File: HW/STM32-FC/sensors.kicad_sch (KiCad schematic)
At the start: 18 parts, among them J5 JST ZH 1.5mm 2P, U6 BMI323, U7 ICM-42688-P, U8 LIS2MDLTR, U9 LPS22HH

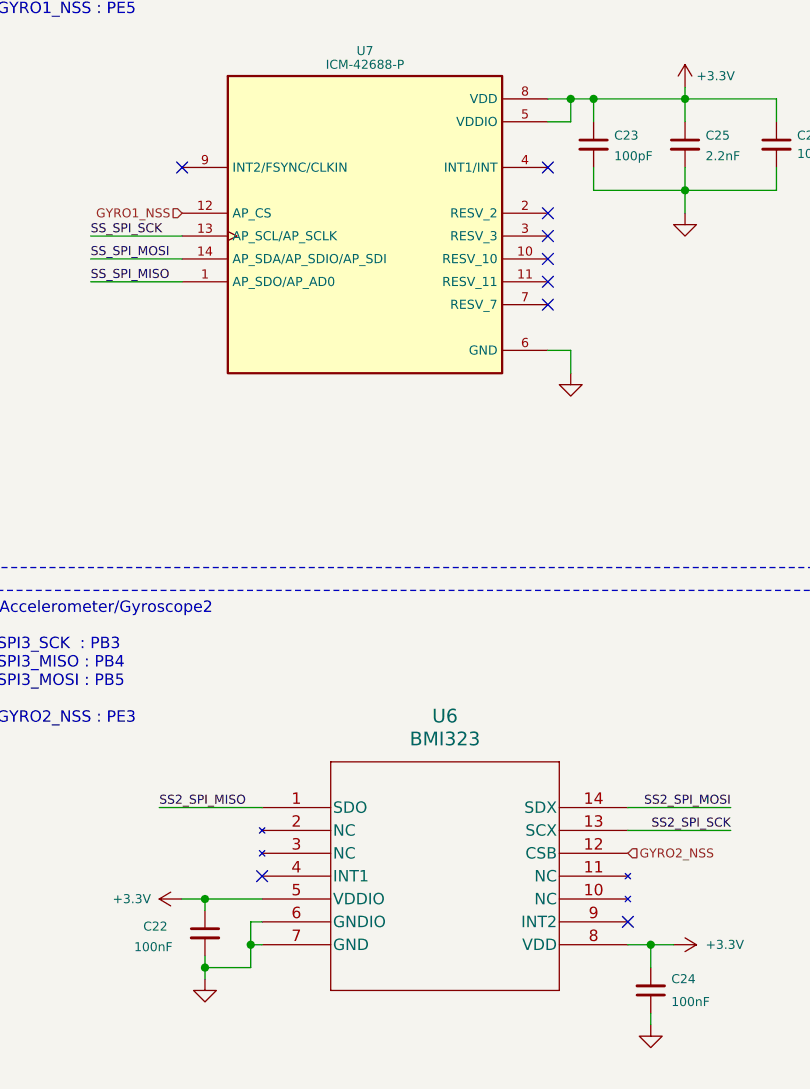
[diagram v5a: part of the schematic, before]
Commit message: SRXL2_readByte() array index out bug fix
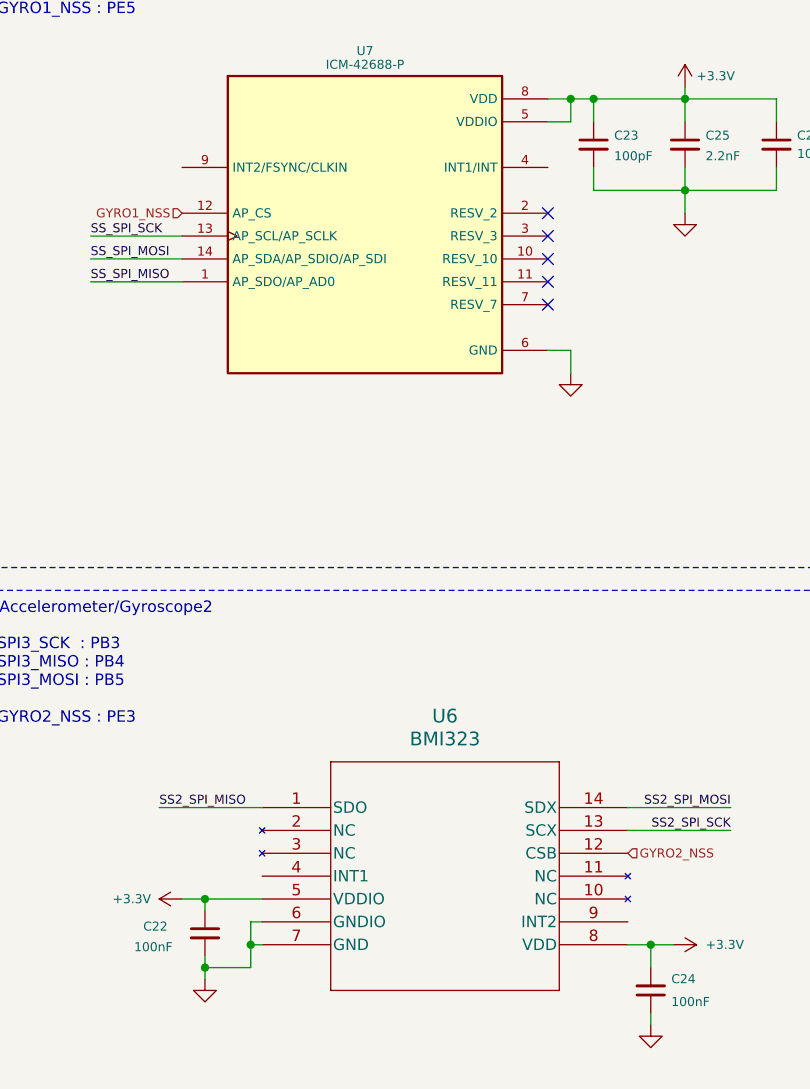
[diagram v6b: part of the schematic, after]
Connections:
- no-connect marks 9 -> 5
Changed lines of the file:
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@@
-	)
-	(no_connect
-		(at 93.98 128.27)
 	)
 	(no_connect
 		(at 85.09 52.07)
-	)
-	(no_connect
-		(at 44.45 44.45)
-	)
-	(no_connect
-		(at 85.09 44.45)
 	)
 	(no_connect
@@
 		(at 85.09 57.15)
 	)
-	(no_connect
-		(at 53.34 123.19)
-	)
 	(wire

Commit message: Log add. backup
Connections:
- net GYRO1_INT: now reaches U7.9 (INT2/FSYNC/CLKIN)
- net GYRO2_INT: now reaches U6.4 (INT1)
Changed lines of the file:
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@@
+		)
+	)
+	(hierarchical_label "GYRO1_INT"
+		(shape output)
+		(at 44.45 44.45 180)
+		(effects
+			(font
+				(size 1 1)
+			)
+			(justify right)
+		)
+	)
+	(hierarchical_label "GYRO2_INT"
+		(shape output)
+		(at 53.34 123.19 180)
+		(effects
+			(font
+				(size 1 1)
+			)
+			(justify right)
 		)
 	)
